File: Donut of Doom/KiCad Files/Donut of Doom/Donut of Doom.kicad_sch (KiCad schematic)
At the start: 30 parts, among them Q1 Q_NMOS_GSD

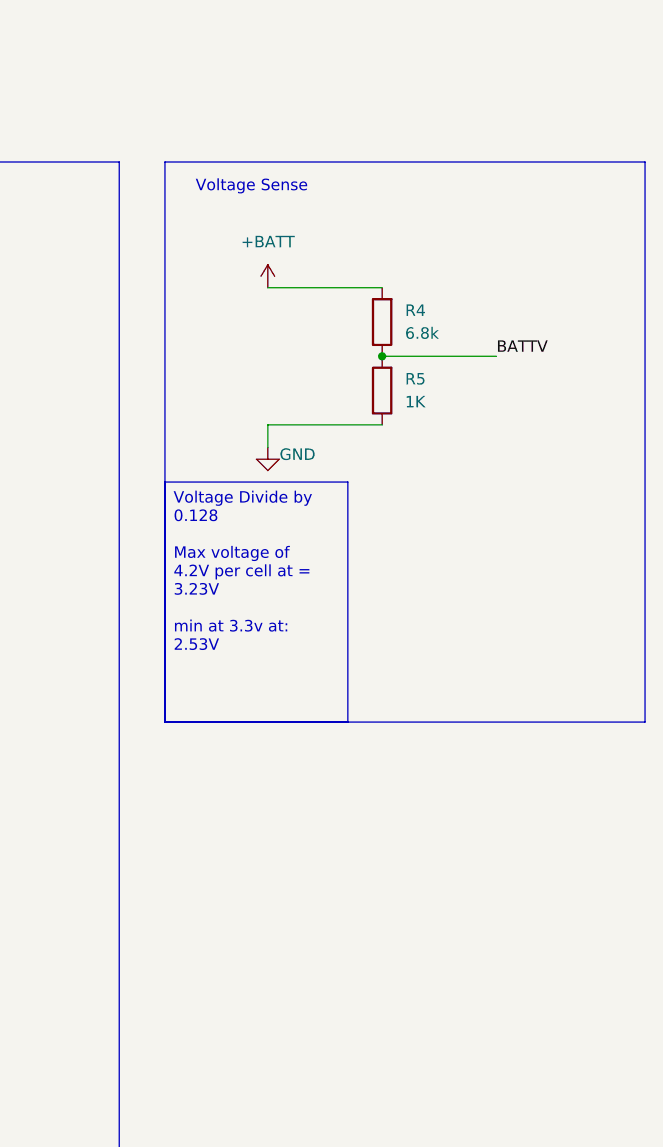
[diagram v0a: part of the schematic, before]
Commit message: New resistor calculations for 6s HV
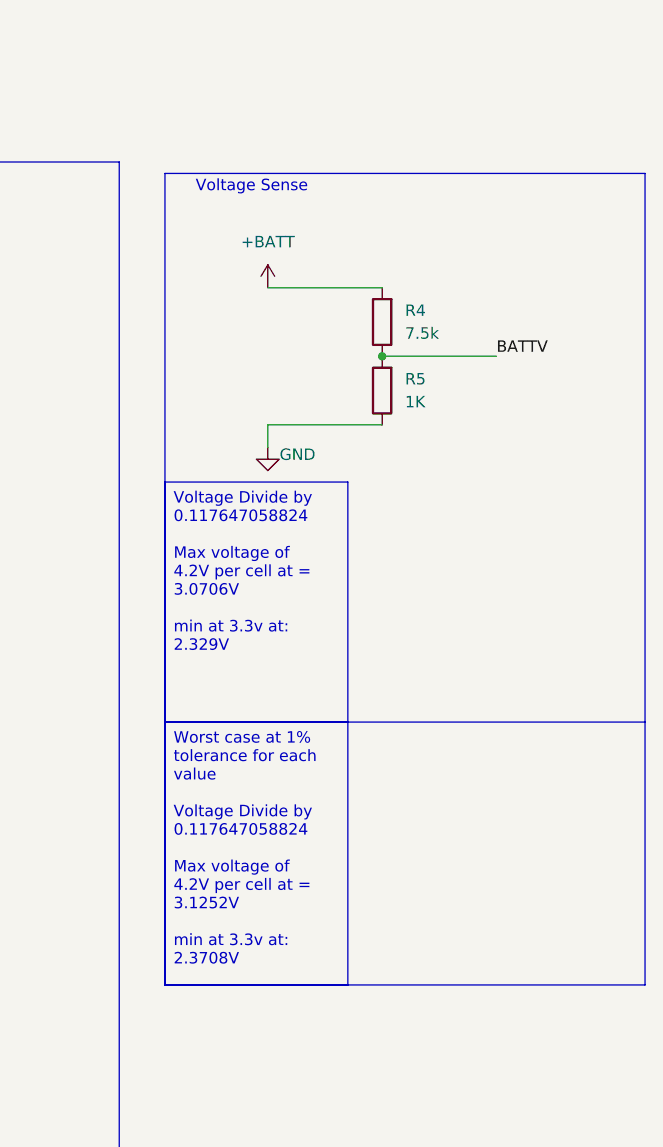
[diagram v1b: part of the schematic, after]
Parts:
- R4: value 6.8k -> 7.5k
